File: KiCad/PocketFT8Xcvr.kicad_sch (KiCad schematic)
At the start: 55 parts, among them J1 HX8357D, J2 ANT, J3 +12V, J4 SI5351 BRK OUT, Q1 2N3904, Q2 2N3906, Q3 2N7000, Q4 2N7000, U1 MCP3422, U2 Si4735-D60-GU, U3 GVA-84, U4 L7805CV

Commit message: KiCad 8
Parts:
- BAT1: Description_1 (none) -> BATTERY HOLDER COIN 20MM PC PIN
- C1: value 22NF -> 100NF; Field5 (none) -> CAP-07885
- C10, C8, C9: footprint (none) -> 0805
- C11, C21, C3: Field5 (none) -> CAP-08390
- C12, C13, C14, C15: Field5 (none) -> CAP-07886
- C16, C17, C18, C23, C24, C25: Field5 (none) -> CAP-08604
- C19, C20, C4: Field5 (none) -> CAP-07885
- C2, C6, C7: Field5 (none) -> CAP-11015
- C22: footprint (none) -> 0603; Field5 (none) -> CAP-08604
- C26: value (none) -> 47 pf; footprint (none) -> 0603; Field5 (none) -> CAP-08913
- C5: Field5 (none) -> CAP-00868
- D1: footprint (none) -> LED_THT:LED_D5.0mm
- J2: Description_1 (none) -> CONN SMA JACK R/A 50 OHM PCB
- L1, L2: footprint (none) -> Inductor_THT:L_Toroid_Vertical_L10.0mm_W5.0mm_P5.08mm
- Q1: Description_1 (none) -> TRANS NPN 40V TO-92
- Q2: Description_1 (none) -> TRANS PNP 40V TO-92
- Q3, Q4: Description_1 (none) -> MOSFET N-CH 60V 200MA TO-92
- R7: footprint (none) -> 2010
- TN: footprint (none) -> teensy:Teensy41
- U1: footprint (none) -> mcp3422
- U4: Description_1 (none) -> IC REG LINEAR 5V 1.5A TO220AB
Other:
- moved on the sheet: J1

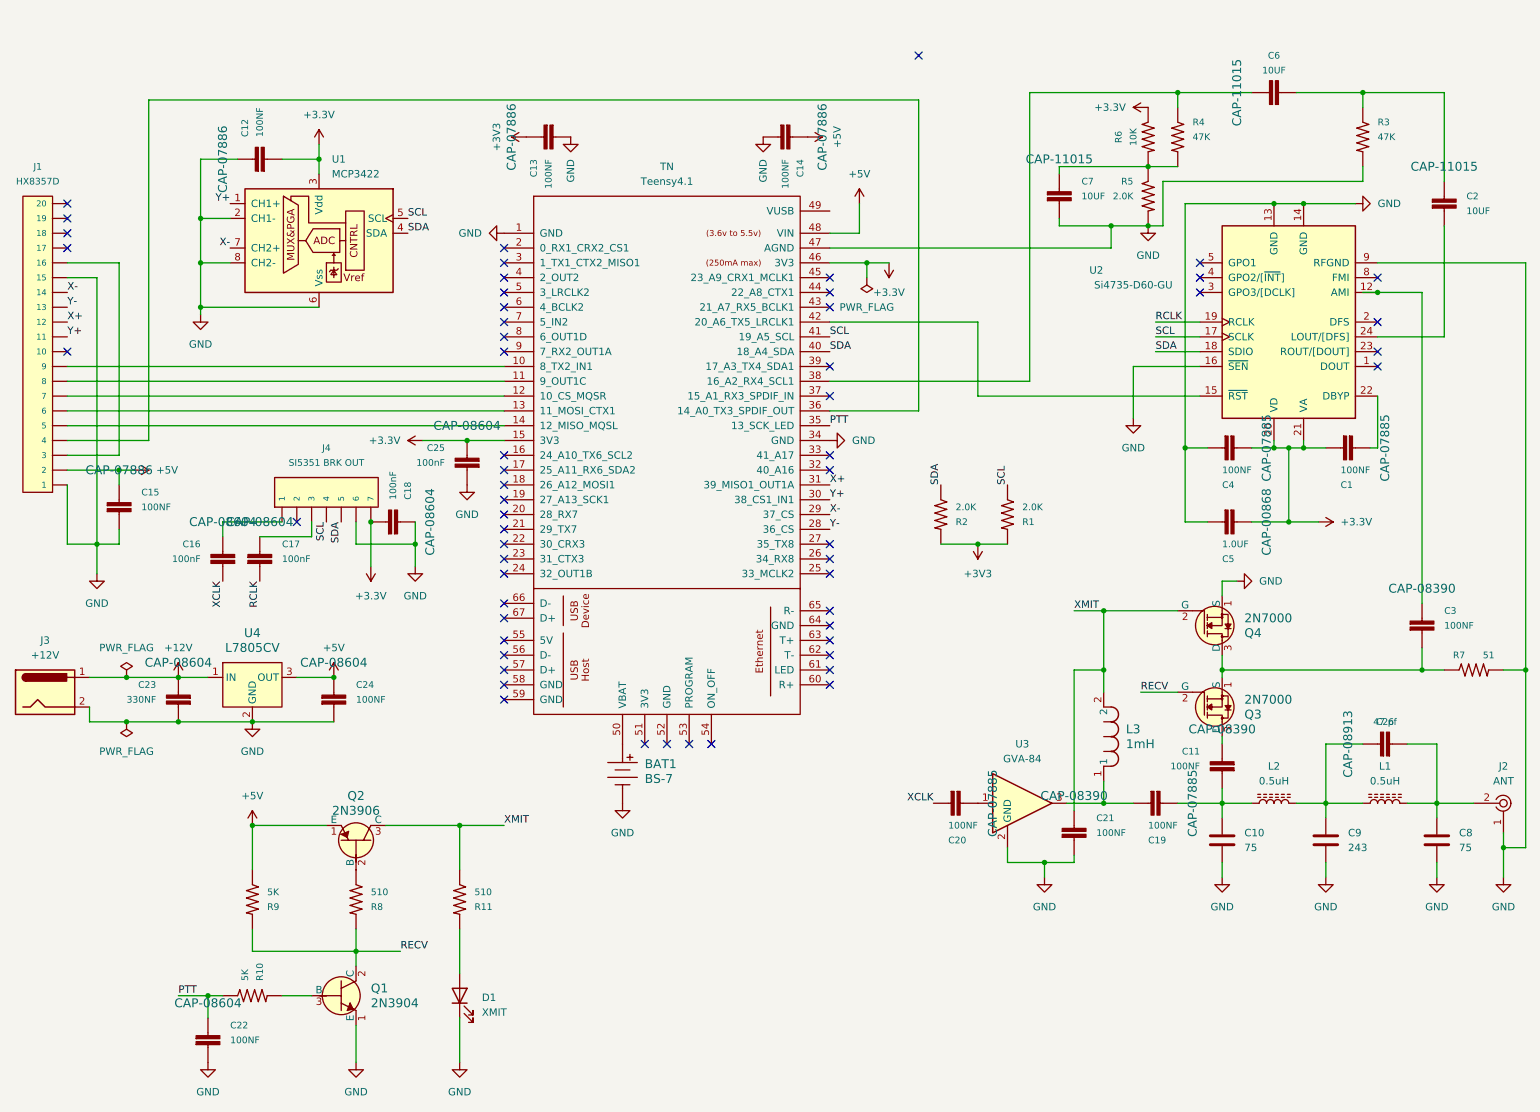
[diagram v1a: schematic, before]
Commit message: Schematic passes Electrical Rules Check (ERC)
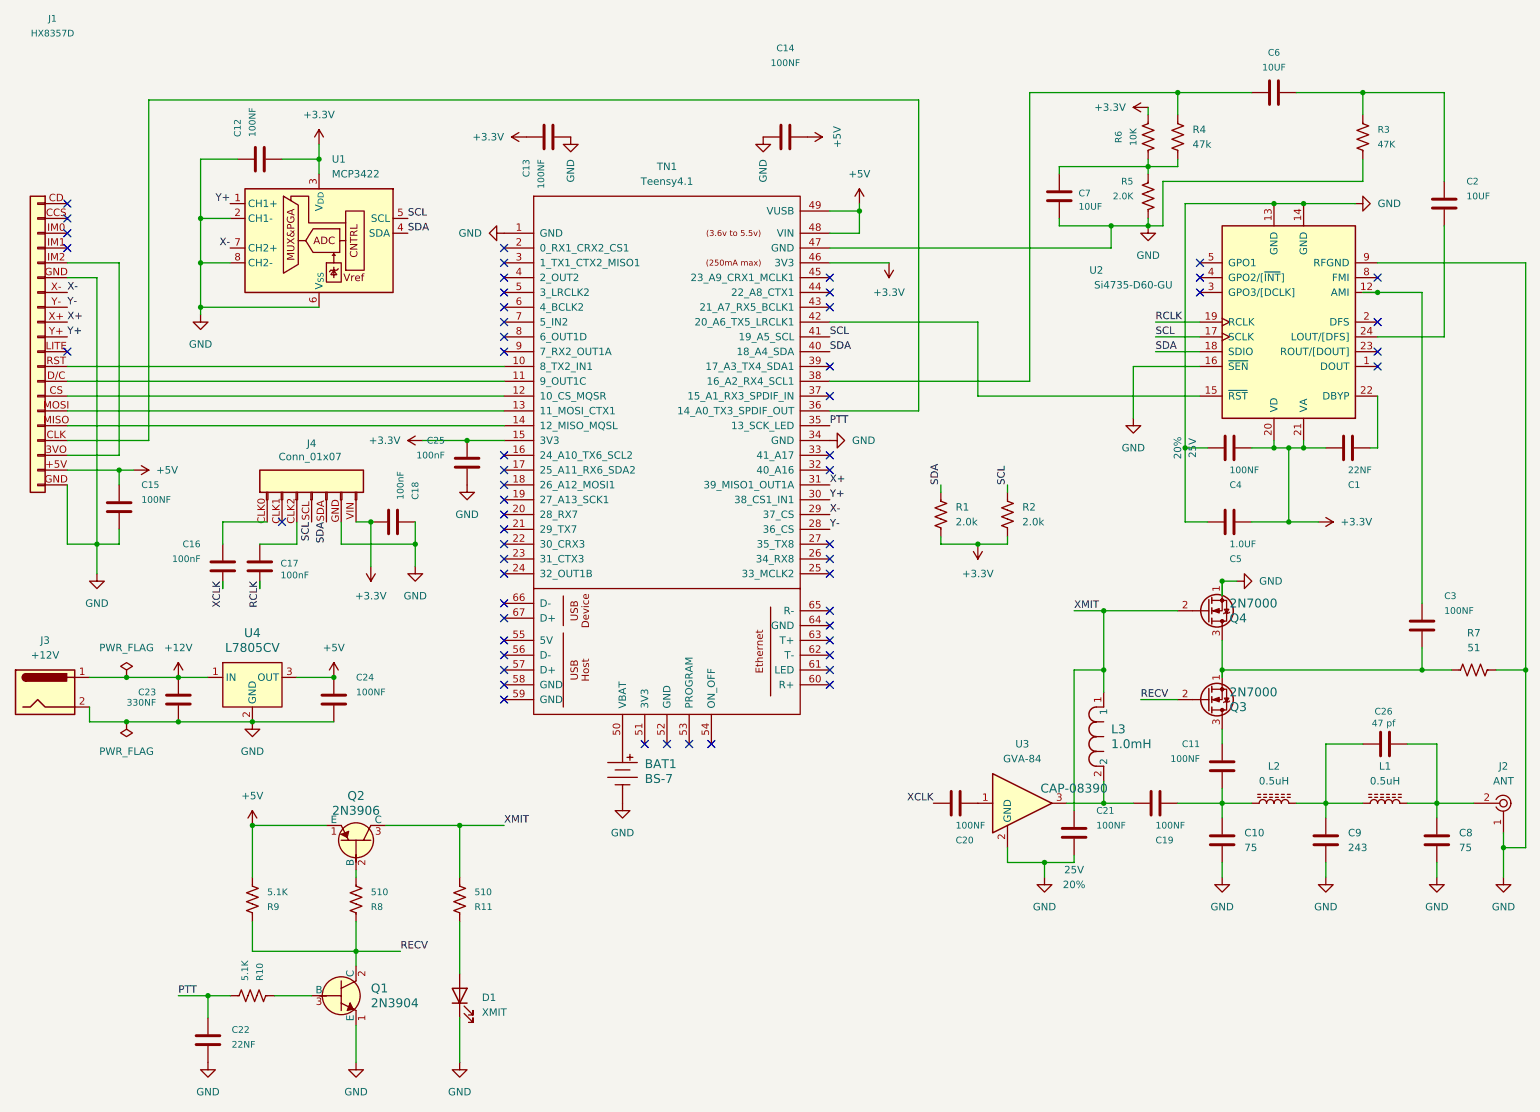
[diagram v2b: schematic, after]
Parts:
- removed J4: SI5351 BRK OUT, 1X07, symbol SparkFun-Connectors:CONN_07
- removed R1, R2: 2.0K, 0603, symbol SparkFun-Resistors:2.0KOHM-0603-1_10W-5%
- removed R4: 47K, 0603, symbol SparkFun-Resistors:47KOHM-0603-1_10W-1%
- removed R7: 51, 2010, symbol SparkFun-Resistors:510OHM-2010-1_2W-5%
- added J4: Conn_01x07, SparkFun-Connector:1x07, symbol SparkFun-Connector:Conn_01x07
- added R1, R2: 2.0k, SparkFun-Resistor:R_0603_1608Metric, symbol SparkFun-Resistor:2.0k_0603
- added R4: 47k, SparkFun-Resistor:R_0603_1608Metric, symbol SparkFun-Resistor:47k_0603
- added R7: 51, 0603, symbol SparkFun-Resistor:R
- C1: value 100NF -> 22NF; footprint 0603 -> SparkFun-Capacitor:C_0603_1608Metric; symbol SparkFun-Capacitors:22NF_22_000PF-0603-50V-10% -> SparkFun-Capacitor:0.1uF_0603_25V_20%; PROD_ID (none) -> CAP-00810; Tolerance (none) -> 20%; Voltage (none) -> 25V
- C11, C21, C3: footprint 0603 -> SparkFun-Capacitor:C_0603_1608Metric; symbol SparkFun-Capacitors:0.1UF-0603-100V-10% -> SparkFun-Capacitor:0.1uF_0603_25V_20%; PROD_ID (none) -> CAP-00810; Tolerance (none) -> 20%; Voltage (none) -> 25V
- C12, C13, C14, C15: footprint 0603 -> SparkFun-Capacitor:C_0603_1608Metric; symbol SparkFun-Capacitors:1.0NF_1000PF-0603-50V-10% -> SparkFun-Capacitor:0.1uF_0603_25V_20%; PROD_ID (none) -> CAP-00810; Tolerance (none) -> 20%; Voltage (none) -> 25V
- C16, C17, C18, C24, C25: footprint 0603 -> SparkFun-Capacitor:C_0603_1608Metric; symbol SparkFun-Capacitors:0.1UF-0603-25V-5% -> SparkFun-Capacitor:0.1uF_0603_25V_20%; PROD_ID (none) -> CAP-00810; Tolerance (none) -> 20%; Voltage (none) -> 25V
- C19, C20, C4: footprint 0603 -> SparkFun-Capacitor:C_0603_1608Metric; symbol SparkFun-Capacitors:22NF_22_000PF-0603-50V-10% -> SparkFun-Capacitor:0.1uF_0603_25V_20%; PROD_ID (none) -> CAP-00810; Tolerance (none) -> 20%; Voltage (none) -> 25V
- C2, C6, C7: footprint 0603 -> SparkFun-Capacitor:C_0603_1608Metric; symbol SparkFun-Capacitors:10UF-0603-6.3V-20% -> SparkFun-Capacitor:10uF_0603_6.3V_20%; Field5 CAP-11015 -> (none); PROD_ID (none) -> CAP-11015; Tolerance (none) -> 20%; Voltage (none) -> 6.3V
- C22: value 100NF -> 22NF; footprint 0603 -> SparkFun-Capacitor:C_0603_1608Metric; symbol SparkFun-Capacitors:0.1UF-0603-25V-5% -> SparkFun-Capacitor:0.1uF_0603_25V_20%; PROD_ID (none) -> CAP-00810; Tolerance (none) -> 20%; Voltage (none) -> 25V
- C23: symbol SparkFun-Capacitors:0.1UF-0603-25V-5% -> Device:C; Field5 CAP-08604 -> (none)
- C26: footprint 0603 -> Capacitor_SMD:C_0805_2012Metric; symbol SparkFun-Capacitors:47PF-0603-50V-5% -> SparkFun-Capacitor:47pF_0603_50V_5%; PROD_ID (none) -> CAP-08913; Tolerance (none) -> 1%; Voltage (none) -> 100v
- C5: footprint 0603 -> SparkFun-Capacitor:C_0603_1608Metric; symbol SparkFun-Capacitors:1.0UF-0603-16V-10% -> SparkFun-Capacitor:1.0uF_0603_16V_10%; Field5 CAP-00868 -> (none); PROD_ID (none) -> CAP-13930; Tolerance (none) -> 10%; Voltage (none) -> 16V
- J1: footprint 1X20 -> SparkFun-Connector:1x20; symbol SparkFun-Connectors:CONN_20 -> SparkFun-Connector:Conn_01x20
- L3: value 1mH -> 1.0mH; Digi-Key_PN (none) -> RLB9012-102KL-N
- Q3, Q4: footprint digikey-footprints:TO-92-3 -> Package_TO_SOT_THT:TO-92_Inline; symbol dk_Transistors-FETs-MOSFETs-Single:2N7000 -> Transistor_FET:2N7000; Category Discrete Semiconductor Products -> (none); DK_Datasheet_Link https://www.onsemi.com/pub/Collateral/NDS7002A-D.PDF -> (none); DK_Detail_Page /product-detail/en/on-semiconductor/2N7000/2N7000FS-ND/2442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 -> (none); Description_1 MOSFET N-CH 60V 200MA TO-92 -> (none); Digi-Key_PN 2N7000FS-ND -> (none); Family Transistors - FETs, MOSFETs - Single -> (none); MPN 2N7000 -> (none); Manufacturer ON Semiconductor -> (none); Status Active -> (none)
- R10, R9: value 5K -> 5.1K; footprint 0603 -> SparkFun-Resistor:R_0603_1608Metric; symbol SparkFun-Resistors:2.0KOHM-0603-1_10W-5% -> SparkFun-Resistor:5.1k_0603; PROD_ID (none) -> RES-12083
- R11, R5, R8: footprint 0603 -> SparkFun-Resistor:R_0603_1608Metric; symbol SparkFun-Resistors:2.0KOHM-0603-1_10W-5% -> SparkFun-Resistor:2.0k_0603; PROD_ID (none) -> RES-08296
- R3: footprint 0603 -> SparkFun-Resistor:R_0603_1608Metric; symbol SparkFun-Resistors:47KOHM-0603-1_10W-1% -> SparkFun-Resistor:47k_0603; PROD_ID (none) -> RES-07871
- R6: footprint 0603 -> SparkFun-Resistor:R_0603_1608Metric; symbol SparkFun-Resistors:10KOHM-0603-1_10W-1% -> SparkFun-Resistor:10k_0603; PROD_ID (none) -> RES-00824
- TN1: renamed from TN; footprint teensy:Teensy41 -> (none); symbol teensy:Teensy4.1 -> teensy1:Teensy4.1
- U1: footprint mcp3422 -> Package_SO:SOIC-8_3.9x4.9mm_P1.27mm; symbol Analog_ADC:MCP3422 -> Analog_ADC:MCP3422Axx-xSN
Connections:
- net +3V3 is gone; now on net +3.3V: C13.1
- net +3.3V: now also R6.2, J4.VIN, R1.2, R2.2; no longer R6.1
- net +5V: now also J1.+5V (Pin_19), R9.2, TN1.49 (VUSB); no longer J1.2, R9.1
- net GND: now also J1.GND (Pin_6), R3.1, R5.1, J4.GND, R7.1; no longer J1.1, J1.15, R3.2, R5.2
- net PTT: now also R10.2; no longer R10.1
- net RECV: now also R8.1, R9.1; no longer R8.2, R9.2
- net SCL: now also J4.SCL, R2.1
- net SDA: now also J4.SDA, R1.1
- net X+: now also J1.X+ (Pin_9); no longer J1.12
- net X-: now also J1.X- (Pin_7); no longer J1.14
- net XMIT: now also L3.1, R11.2; no longer L3.2, R11.1
- net Y+: now also J1.Y+ (Pin_10); no longer J1.11
- net Y-: now also J1.Y- (Pin_8); no longer J1.13
- net at Q1.3 (B): now also R10.1; no longer R10.2
- net at C6.1, TN1.38 (16_A2_RX4_SCL1): now also R4.2
- net at C3.2, Q3.1 (S), Q4.3 (D): now also R7.2
- net at Q2.2 (B): now also R8.2; no longer R8.1
- net at C19.2, U3.3: now also L3.2; no longer L3.1
- net at C16.1: now also J4.CLK0
- net at C17.1: now also J4.CLK2
- net at C2.1, C6.2: now also R3.2; no longer R3.1
- net at D1.2 (A): now also R11.1; no longer R11.2
- net at TN1.36 (14_A0_TX3_SPDIF_OUT): now also J1.CLK (Pin_17); no longer J1.4
- net at TN1.14 (12_MISO_MQSL): now also J1.MISO; no longer J1.5
- net at TN1.13 (11_MOSI_CTX1): now also J1.MOSI (Pin_15); no longer J1.6
- net at TN1.12 (10_CS_MQSR): now also J1.CS (Pin_14); no longer J1.7
- net at TN1.11 (9_OUT1C): now also J1.D/C (Pin_13); no longer J1.8
- net at TN1.10 (8_TX2_IN1): now also J1.RST (Pin_12); no longer J1.9
- new net: C7.1, R4.1, R5.2, R6.1
- new net: J1.3VO (Pin_18), J1.IM2 (Pin_5)
- no-connect marks 58 -> 57
